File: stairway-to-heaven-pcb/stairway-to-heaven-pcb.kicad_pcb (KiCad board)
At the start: 4 copper layers, 99.8 x 97.3 mm, 114 parts, among them J1 Conn_01x04_Male, J10 Conn_01x04_Male, J11 Conn_01x04_Male, J12 Conn_01x04_Male, J13 Conn_01x04_Male, J14 Conn_01x04_Male, J15 PJ-063AH, J2 Conn_01x04_Male, J3 Conn_01x04_Male, J4 Conn_01x04_Male, J5 Conn_01x04_Male, J6 Conn_01x04_Male, J7 Conn_01x04_Male, J8 Conn_01x04_Male, J9 Conn_01x04_Male, Q1 FDN337N, Q10 FDN337N, Q11 FDN337N, Q12 FDN337N, Q13 FDN337N, Q14 FDN337N, Q15 FDN337N, Q16 FDN337N, Q17 FDN337N, Q18 FDN337N, Q19 FDN337N, Q2 FDN337N, Q20 FDN337N, Q21 FDN337N, Q22 FDN337N, Q23 FDN337N, Q24 FDN337N, Q25 FDN337N, Q26 FDN337N, Q27 FDN337N, Q28 FDN337N, Q29 FDN337N, Q3 FDN337N, Q30 FDN337N, Q31 FDN337N, Q32 FDN337N, Q33 FDN337N, Q34 FDN337N, Q35 FDN337N, Q36 FDN337N, Q37 FDN337N, Q38 FDN337N, Q39 FDN337N, Q4 FDN337N, Q40 FDN337N, Q41 FDN337N, Q42 FDN337N, Q5 FDN337N, Q6 FDN337N, Q7 FDN337N, Q8 FDN337N, Q9 FDN337N, U1 MEGA_PRO_EMBED_CH340G_{slash}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, U2 LM2575T-5.0

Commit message: Silks, small mods
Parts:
- moved C3 1.15 mm to (168.4, 134.7), turned to 90 degrees
- moved D1 0.92 mm to (175.6, 128.4)
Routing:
- net +5V: track 228.0 -> 210.6 mm
- net /LED2G_EN: track 46.9 -> 44.5 mm
- net /LED9R_EN: track 50.4 -> 48.9 mm
- net /LED5B_EN: track 36.1 -> 34.9 mm
- net /LED3R_EN: track 53.1 -> 52.2 mm
- net /LED3G_EN: track 52.7 -> 51.8 mm
- net /LED3B_EN: track 59.2 -> 58.4 mm
- net /LED1G_EN: track 70.7 -> 70.1 mm
- net /LED1R_EN: track 76.3 -> 75.7 mm
- net /LED1B_EN: track 80.2 -> 79.7 mm
- net GND: vias 464 -> 411
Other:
- board text added: "Led1"
- board text added: "Led10"
- board text added: "Led11"
- board text added: "Led12"
- board text added: "Led13"
- board text added: "Led14"
- board text added: "Led2"
- board text added: "Led3"
- board text added: "Led4"
- board text added: "Led5"
- board text added: "Led6"
- board text added: "Led7"
- board text added: "Led8"
- board text added: "Led9"
- board text added: "Stairway to Heaven - Sami Sorell"

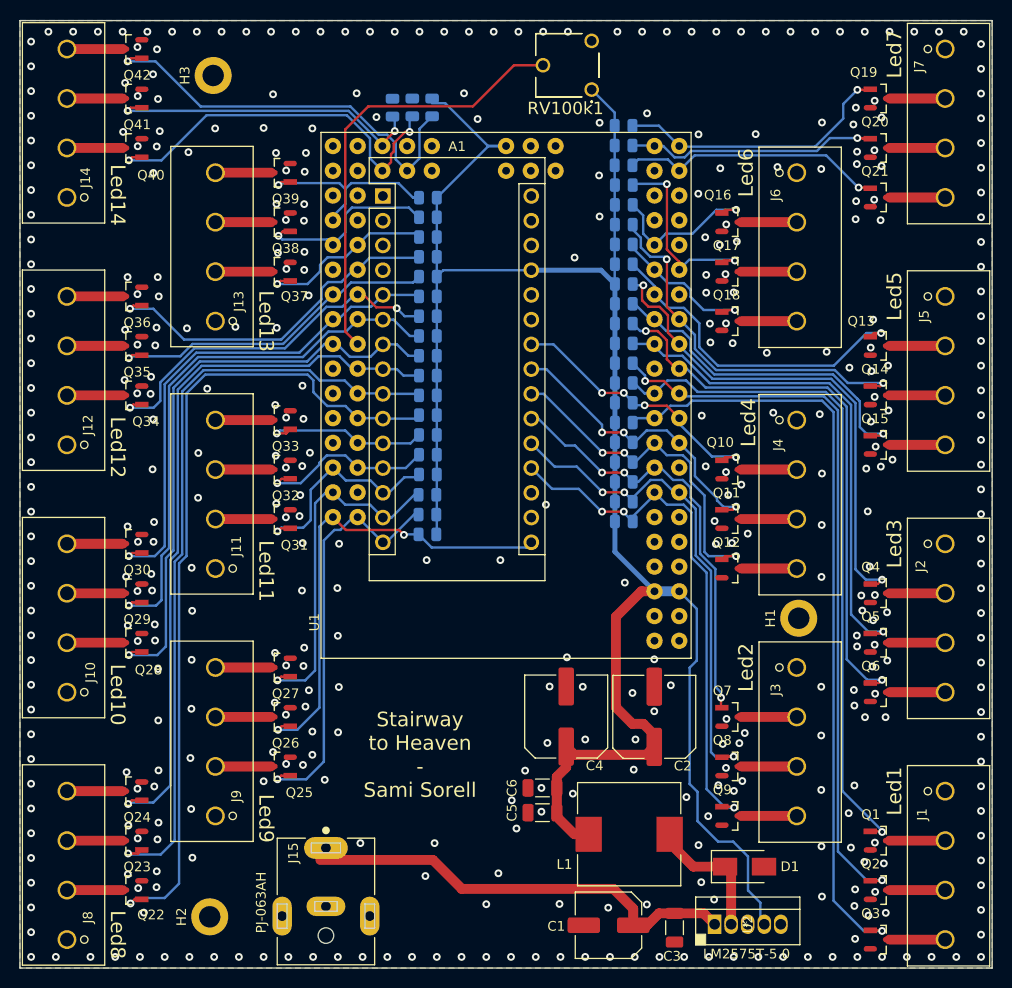
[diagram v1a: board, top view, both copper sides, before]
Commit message: Add terminal for sensors
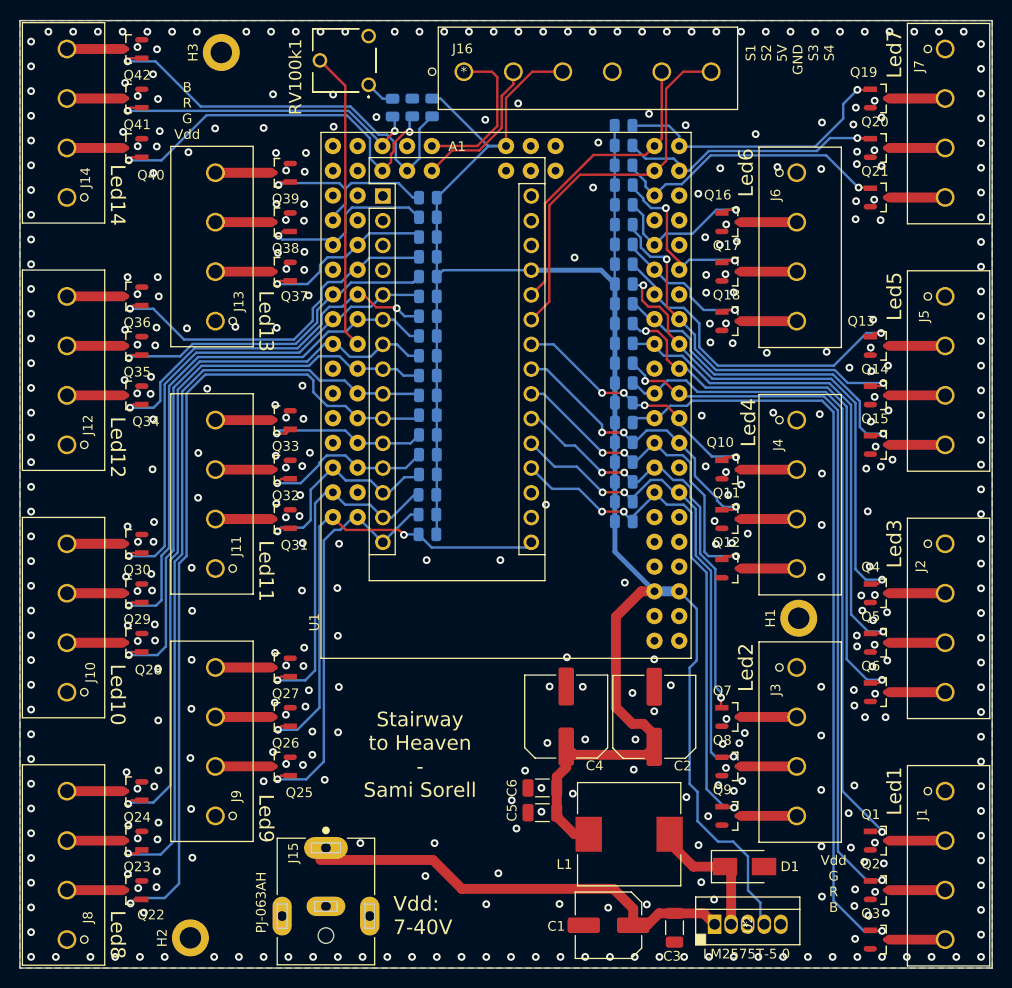
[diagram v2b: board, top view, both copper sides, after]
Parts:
- added J16: Conn_01x06_Male, ScrewTerminal-5_08:ScrewTerminal-5_08-6, F.Cu at (146.8, 46.8)
- moved RV100k1 22.9 mm to (137.0, 48.1)
- moved H2 2.93 mm to (118.7, 135.7)
- moved H3 2.51 mm to (121.9, 44.8)
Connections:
- A1 pad 25: unconnected-(A1-Pad25) -> /SENSOR4
- A1 pad 26: unconnected-(A1-Pad26) -> /SENSOR3
- U1 pad D26: unconnected-(U1-PadD26) -> /LED7B_EN
- U1 pad D28: unconnected-(U1-PadD28) -> /SENSOR4
- U1 pad D29: /LED7B_EN -> /LED7R_EN
- U1 pad D30: /LED7R_EN -> /SENSOR3
- U1 pad D52: unconnected-(U1-PadD52) -> /SENSOR1
- U1 pad D53: unconnected-(U1-PadD53) -> /SENSOR2
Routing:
- net /SENSOR4: track 0.00 -> 39.1 mm
- net /SENSOR3: track 0.00 -> 31.6 mm
- net /SENSOR1: track 0.00 -> 16.3 mm
- net /SENSOR2: track 0.00 -> 15.3 mm
- net /POT1: track 45.6 -> 30.7 mm
- net +5V: track 210.6 -> 221.0 mm
- net /LED7B_EN: track 27.2 -> 29.3 mm
- net /LED7R_EN: track 25.8 -> 27.3 mm
- net /LED6R_EN: track 20.5 -> 19.1 mm
- net /LED12B_EN: track 36.5 -> 37.3 mm
- net /LED12R_EN: track 34.7 -> 35.5 mm
- net /LED7G_EN: track 28.3 -> 28.9 mm
- net /LED12G_EN: track 37.9 -> 38.5 mm
- net GND: vias 411 -> 408
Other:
- board text added: "B R G Vdd"
- board text added: "S1 S2 5V GND S3 S4"
- board text added: "Vdd G R B"
- board text added: "Vdd: 7-40V"

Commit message: Final touches
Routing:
- net +5V: track 221.0 -> 225.0 mm
